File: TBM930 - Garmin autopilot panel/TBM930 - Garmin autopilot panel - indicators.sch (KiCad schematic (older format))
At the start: 26 parts

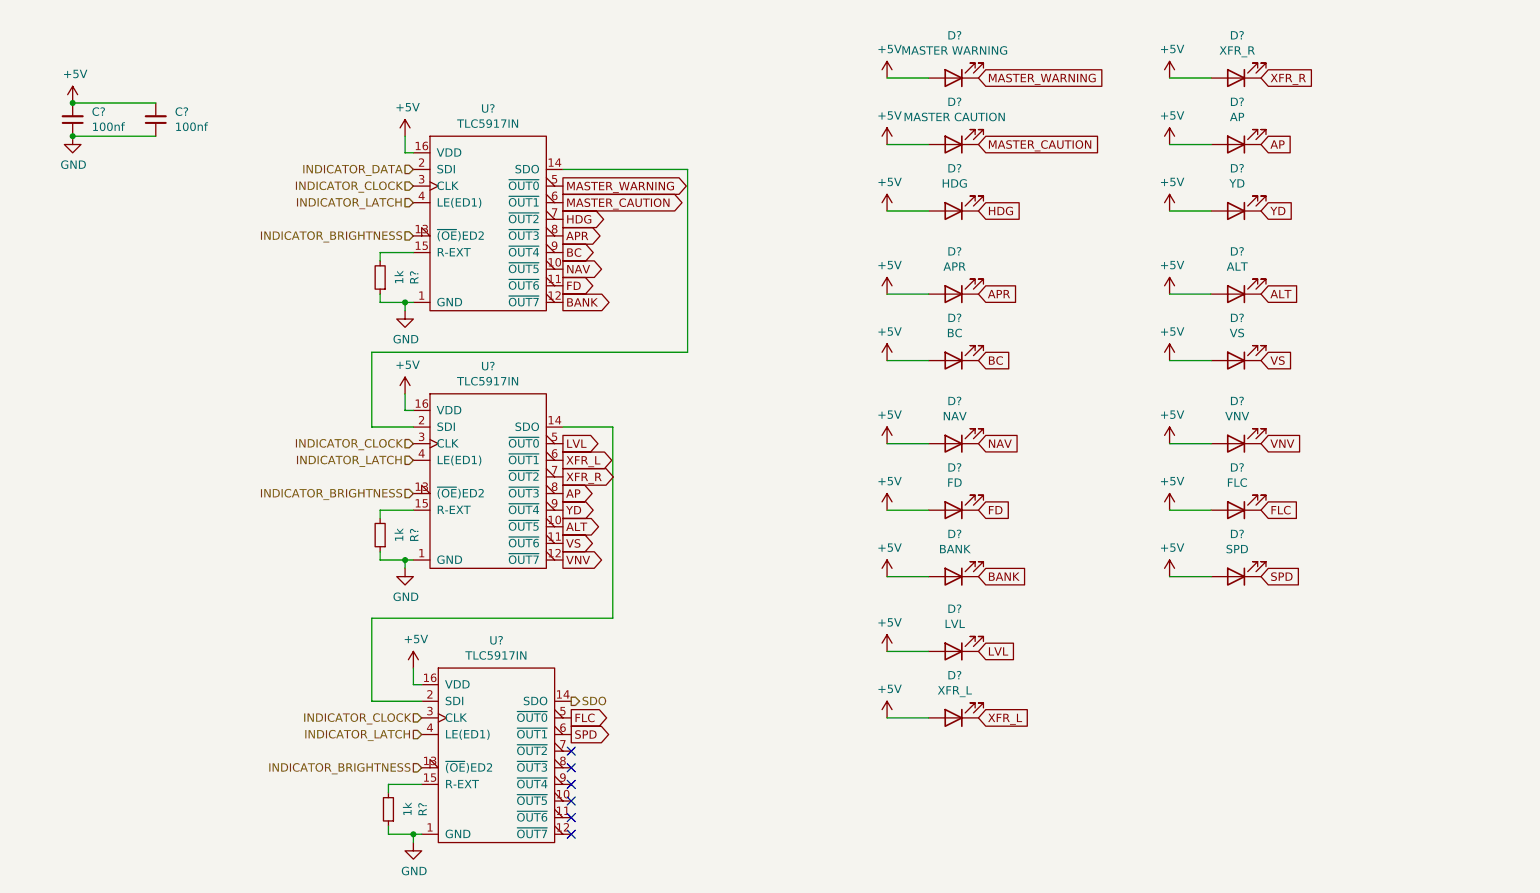
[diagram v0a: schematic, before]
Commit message: Add all the inputs
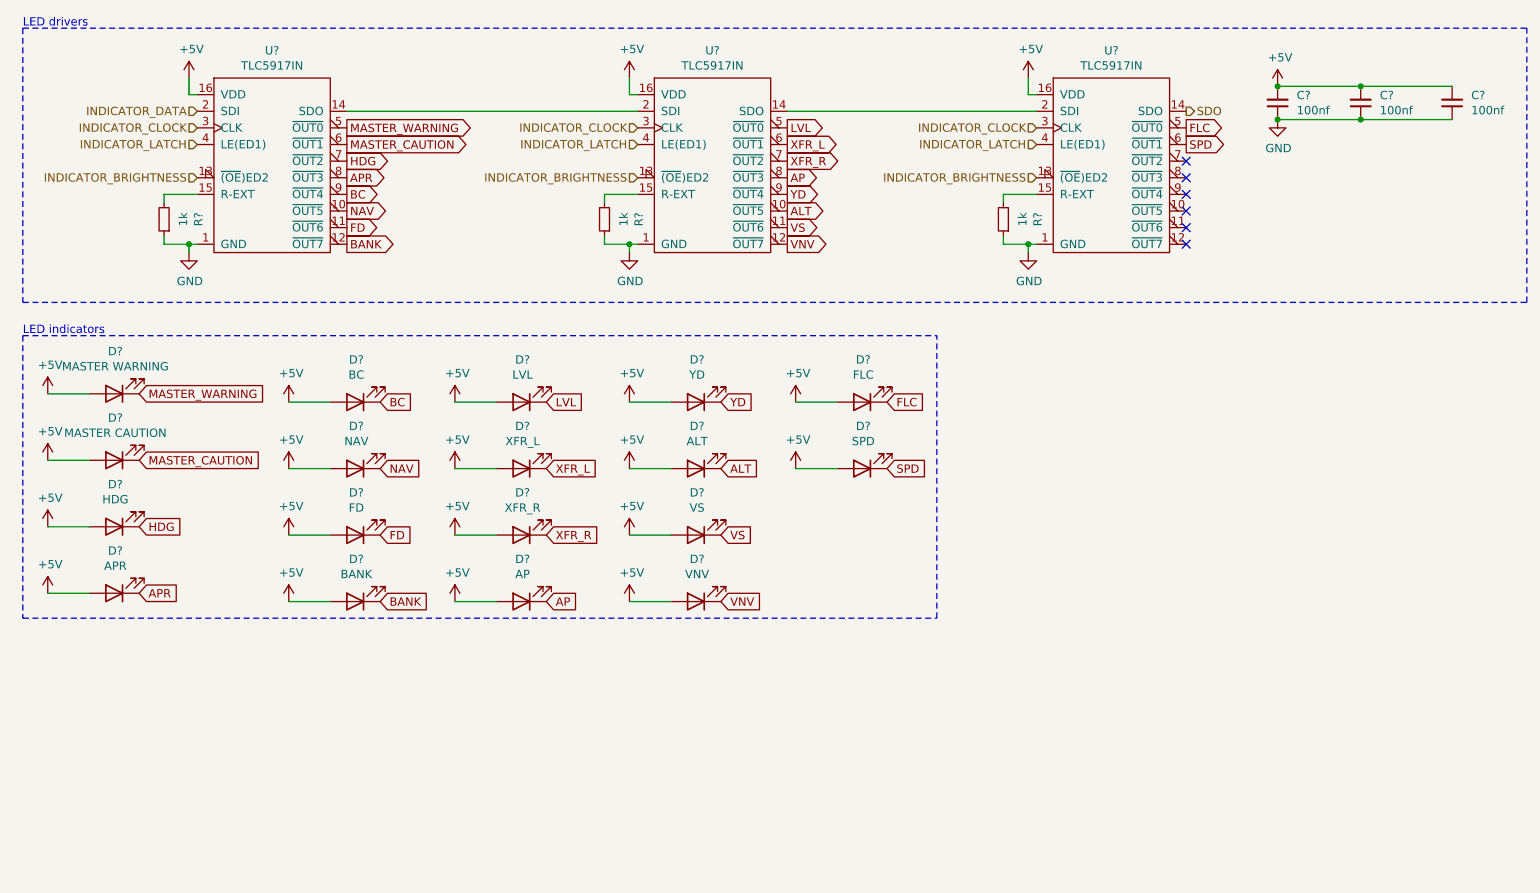
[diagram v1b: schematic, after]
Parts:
- added C?: 100nf, Capacitor_SMD:C_0402_1005Metric, symbol Device:C_Small
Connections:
- net +5V: now also C?.2
- net GND: now also C?.1
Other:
- note added: "LED drivers"
- note added: "LED indicators"
- moved on the sheet: C?, D?, R?, U?
